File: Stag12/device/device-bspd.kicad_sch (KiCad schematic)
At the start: 1 part

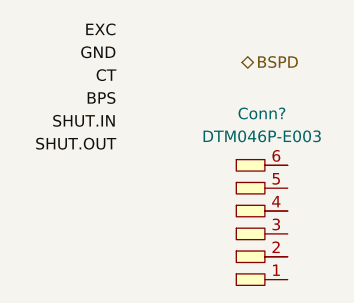
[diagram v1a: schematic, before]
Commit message: Changed EXCs to PWRs
any mention of exc switched to pwr :)
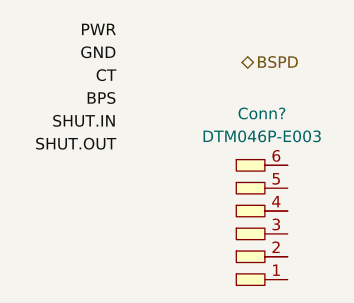
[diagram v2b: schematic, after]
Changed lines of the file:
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@@
 		(title "DEVICE - BSPD")
 	)
-	(label "EXC"
+	(label "PWR"
 		(at 124.46 86.36 180)
 		(effects
